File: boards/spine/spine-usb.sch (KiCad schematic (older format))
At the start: 4 parts, among them P1 USB_B, U1 FT2232H

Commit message: Get the BOM started
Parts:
- L1, L2: MfgId (none) -> CIB21P260NE; MfrId (none) -> Samsung; RefPrice1k (none) -> 0.00906; Vend1 (none) -> Digikey; Vend1Id (none) -> 1276-6342-2-ND
- P1: MfgId (none) -> E8144-B02022-L; MfrId (none) -> Pulse; RefPrice1k (none) -> 0.28; Vend1 (none) -> Digikey; Vend1Id (none) -> 553-2272-ND
- U1: MfgId (none) -> FT2232HL-REEL; MfrId (none) -> FTDI; RefPrice1k (none) -> 3.70; Vend1 (none) -> Digikey; Vend1Id (none) -> 768-1024-1-ND
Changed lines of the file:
@@
 F 1 "FT2232H" H 6650 5700 50  0000 L CNN
 F 2 "" H 5900 3600 50  0000 C CNN
-F 3 "" H 5900 3600 50  0000 C CNN
+F 3 "http://www.ftdichip.com/Support/Documents/DataSheets/ICs/DS_FT2232H.pdf" H 5900 3600 50  0000 C CNN
+F 4 "3.70" H 5900 3600 60  0001 C CNN "RefPrice1k"
+F 5 "768-1024-1-ND" H 5900 3600 60  0001 C CNN "Vend1Id"
+F 6 "FTDI" H 5900 3600 60  0001 C CNN "MfrId"
+F 7 "FT2232HL-REEL" H 5900 3600 60  0001 C CNN "MfgId"
+F 8 "Digikey" H 5900 3600 60  0001 C CNN "Vend1"
 	1    5900 3600
 	1    0    0    -1
@@
 F 1 "USB_B" H 2200 2650 50  0000 C CNN
 F 2 "" V 2200 2350 60  0000 C CNN
-F 3 "" V 2200 2350 60  0000 C CNN
+F 3 "http://productfinder.pulseeng.com/products/datasheets/E8144-B02022-L.PDF" V 2200 2350 60  0001 C CNN
+F 4 "Digikey" H 2250 2450 60  0001 C CNN "Vend1"
+F 5 "553-2272-ND" H 2250 2450 60  0001 C CNN "Vend1Id"
+F 6 "0.28" H 2250 2450 60  0001 C CNN "RefPrice1k"
+F 7 "Pulse" H 2250 2450 60  0001 C CNN "MfrId"
+F 8 "E8144-B02022-L" H 2250 2450 60  0001 C CNN "MfgId"
 	1    2250 2450
 	0    -1   1    0
@@
 FIFO_DATA[0..7]
 $Comp
-L FERRITE_BEAD L1
-U 1 1 56380FD6
-P 2750 1800
-F 0 "L1" H 2900 1850 50  0000 C BNN
-F 1 "FERRITE_BEAD" H 2900 1725 50  0000 C BNN
-F 2 "" H 2750 1950 50  0001 C CNN
-F 3 "" H 2775 1800 60  0000 C CNN
-	1    2750 1800
-	0    1    1    0
-$EndComp
-$Comp
 L FERRITE_BEAD L2
 U 1 1 5638109A
 P 2750 2700
 F 0 "L2" H 2900 2750 50  0000 C BNN
-F 1 "FERRITE_BEAD" H 2900 2625 50  0000 C BNN
+F 1 "FERRITE_BEAD" H 2900 2625 50  0001 C BNN
 F 2 "" H 2750 2850 50  0001 C CNN
-F 3 "" H 2775 2700 60  0000 C CNN
+F 3 "http://www.samsungsem.com/kr/front/downloadcms.do?path=/kr/support/product-search/bead/__icsFiles/afieldfile/2014/11/13&fileName=S_CIB21P110NE.pdf" H 2775 2700 60  0001 C CNN
+F 4 "0.00906" H 2750 2700 60  0001 C CNN "RefPrice1k"
+F 5 "Samsung" H 2750 2700 60  0001 C CNN "MfrId"
+F 6 "CIB21P260NE" H 2750 2700 60  0001 C CNN "MfgId"
+F 7 "Digikey" H 2750 2700 60  0001 C CNN "Vend1"
+F 8 "1276-6342-2-ND" H 2750 2700 60  0001 C CNN "Vend1Id"
 	1    2750 2700
 	0    1    1    0
@@
 Note TI's recommendations on USB grounding and EMI:\nhttp://www.ti.com/sc/docs/apps/msp/intrface/usb/emitest.pdf
 $Comp
-L GND #PWR1
+L GND #PWR01
 U 1 1 563811A6
 P 2150 3250
-F 0 "#PWR1" H 2150 3000 50  0001 C CNN
+F 0 "#PWR01" H 2150 3000 50  0001 C CNN
 F 1 "GND" H 2150 3100 50  0000 C CNN
 F 2 "" H 2150 3250 60  0000 C CNN
@@
 	2150 3200 2750 3200
 Connection ~ 2150 3200
+$Comp
+L FERRITE_BEAD L1
+U 1 1 563F5CD5
+P 2750 1800
+F 0 "L1" H 2900 1850 50  0000 C BNN
+F 1 "FERRITE_BEAD" H 2900 1725 50  0001 C BNN
+F 2 "" H 2750 1950 50  0001 C CNN
+F 3 "http://www.samsungsem.com/kr/front/downloadcms.do?path=/kr/support/product-search/bead/__icsFiles/afieldfile/2014/11/13&fileName=S_CIB21P110NE.pdf" H 2775 1800 60  0001 C CNN
+F 4 "0.00906" H 2750 1800 60  0001 C CNN "RefPrice1k"
+F 5 "Samsung" H 2750 1800 60  0001 C CNN "MfrId"
+F 6 "CIB21P260NE" H 2750 1800 60  0001 C CNN "MfgId"
+F 7 "Digikey" H 2750 1800 60  0001 C CNN "Vend1"
+F 8 "1276-6342-2-ND" H 2750 1800 60  0001 C CNN "Vend1Id"
+	1    2750 1800
+	0    1    1    0
+$EndComp
 $EndSCHEMATC

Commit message: Fuss with the USB
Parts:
- removed L2: FERRITE_BEAD, symbol FERRITE_BEAD
- added C? (x2): 0.1uF, symbol C
- added C? (x2): 10uF, symbol C
- added FB2: Ferrite bead, symbol FERRITE_BEAD
- added R? (x2): 4.7k, symbol R
- added R?: 10k, symbol R
- added R?: 12k 1%, symbol R
- FB1: renamed from L1; value FERRITE_BEAD -> Ferrite bead
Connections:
- net labels added: +3V3, VBUS_OUT, VBUS_SENSE
- wire segments 15 -> 68
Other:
- note added: "Todo: pick an ESD solution"
- note removed: "Note TI's recommendations on USB grounding and EMI:\nhttp://www.ti.com/sc/docs/apps/msp/intrface/usb/emitest.pdf"
- moved on the sheet: FB1, P1, U1

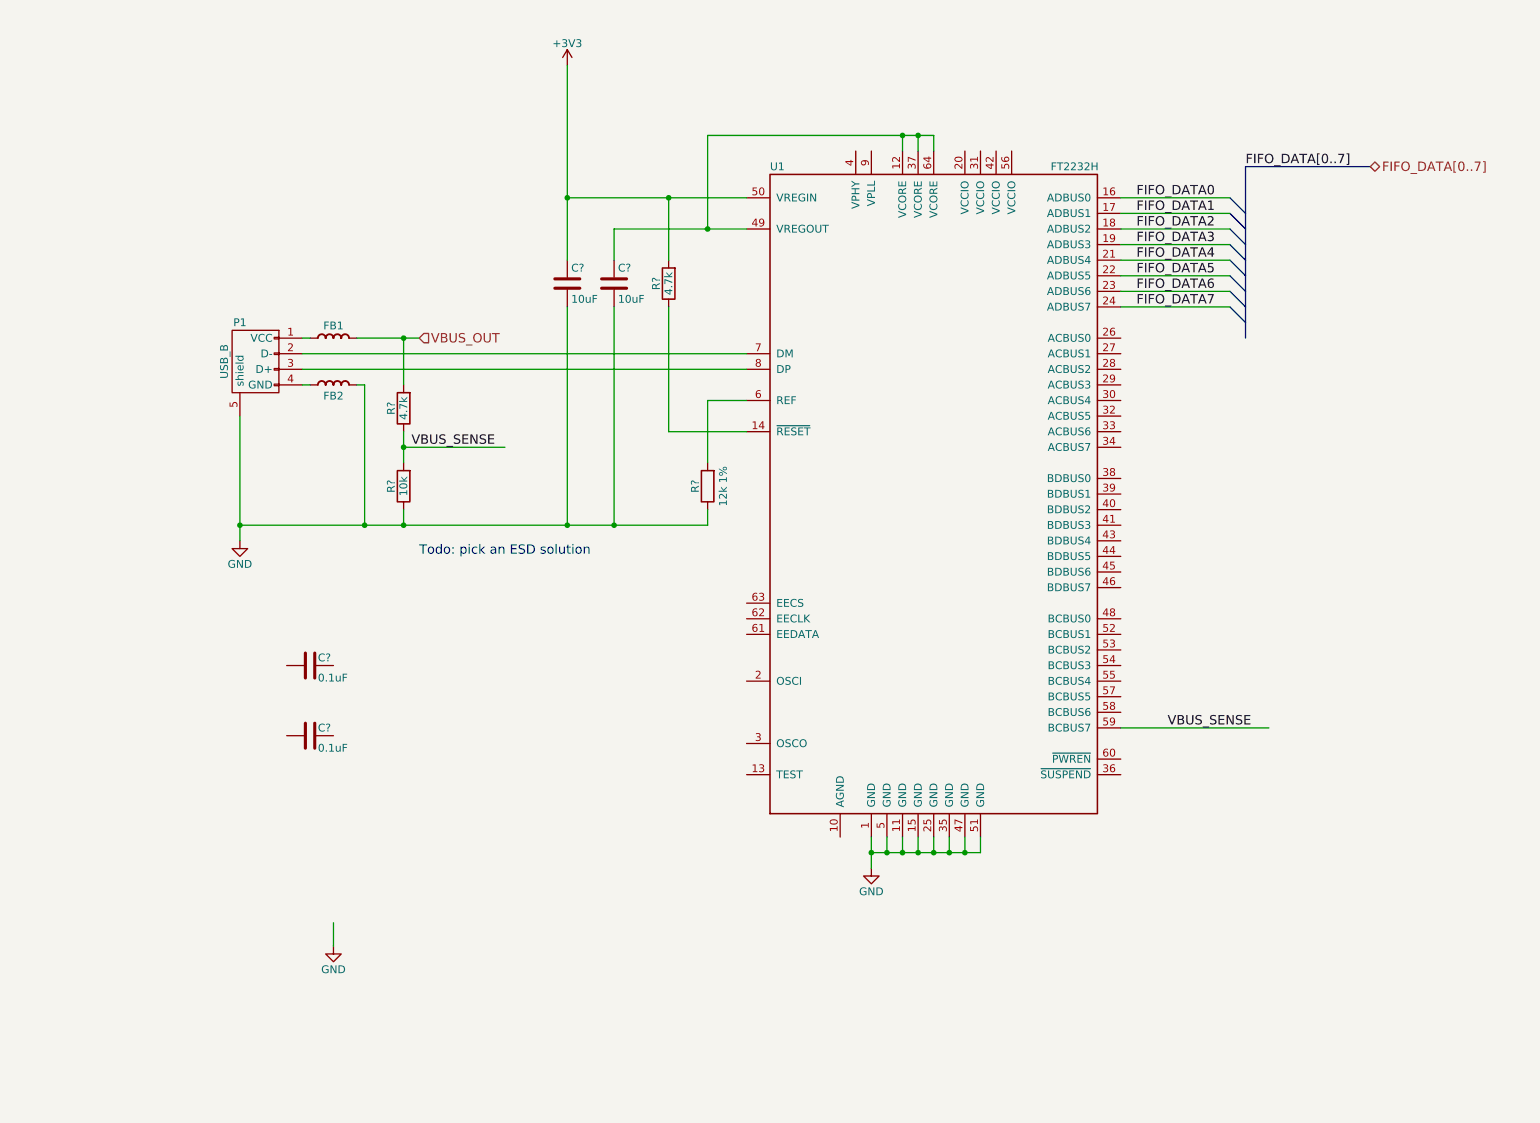
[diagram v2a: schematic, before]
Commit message: USB port: ESD, crystal, eeprom
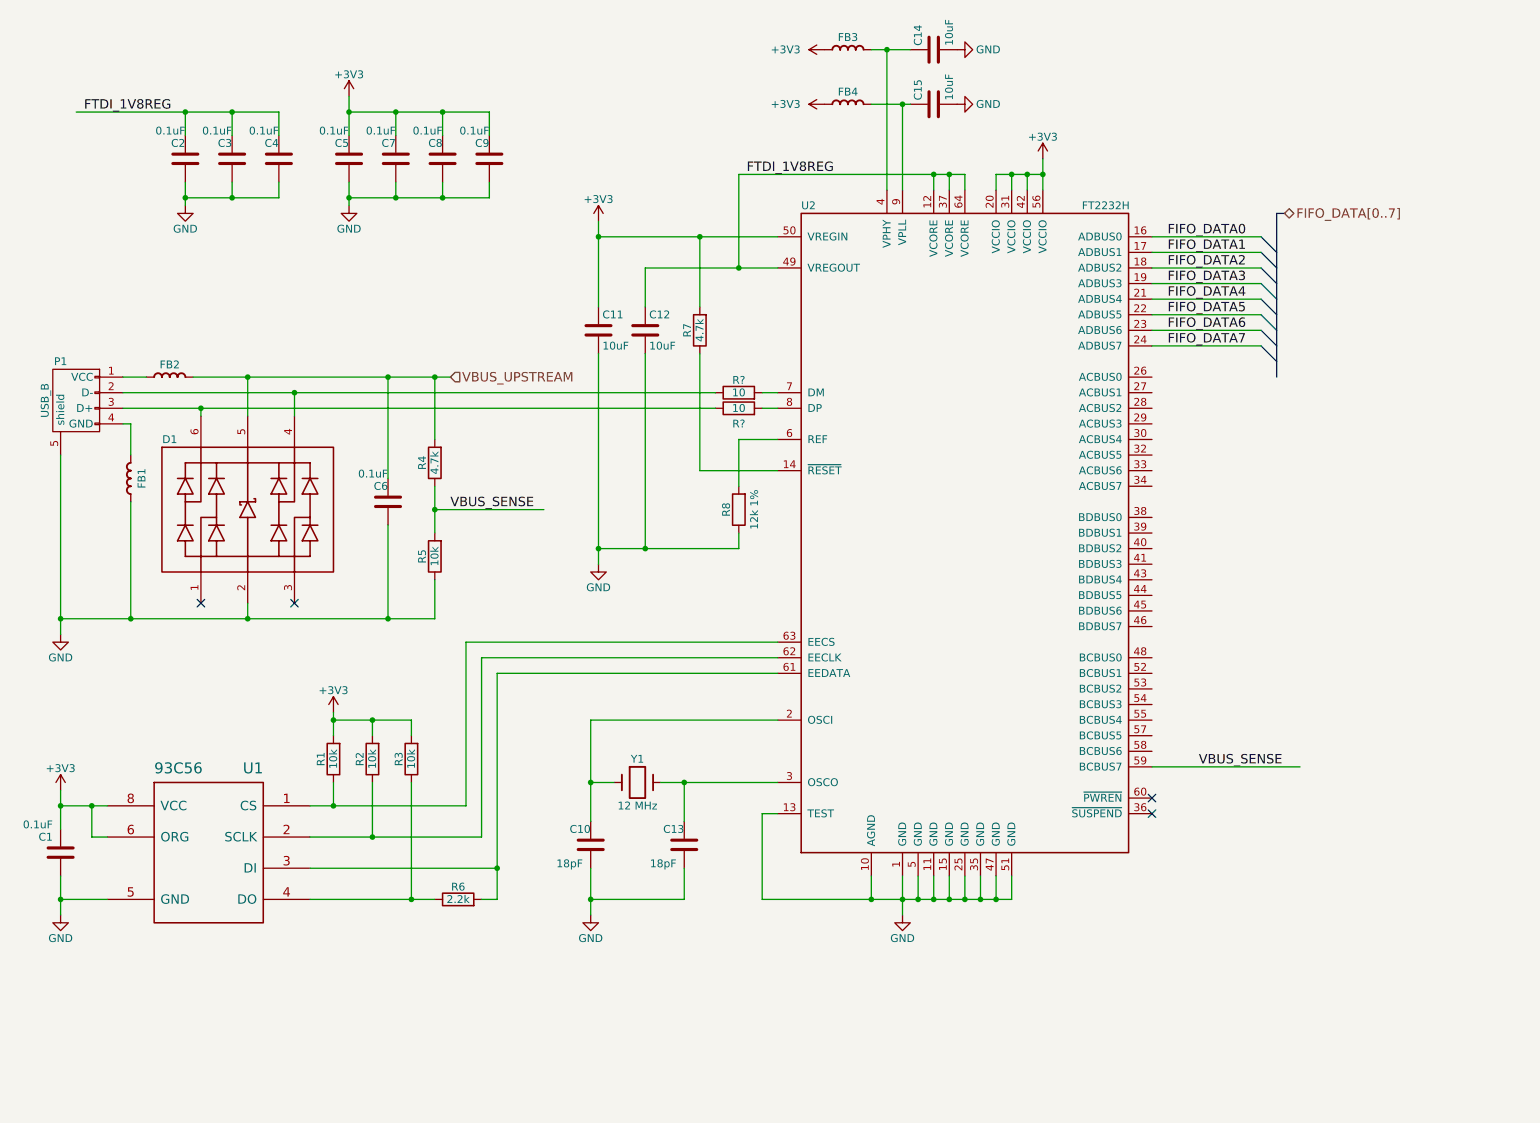
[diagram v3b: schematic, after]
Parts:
- removed C?: 0.1uF, symbol C
- removed C?: 10uF, symbol C
- added C1, C2, C3, C4, C5, C7, C8, C9: 0.1uF, symbol C
- added C10, C13: 18pF, symbol C
- added C11, C14, C15: 10uF, symbol C
- added D1: TVS DIODE 5.5VWM, symbol TVS_QUAD_STEERING
- added FB3, FB4: Ferrite bead, symbol FERRITE_BEAD
- added R1, R2, R3: 10k, symbol R
- added R6: 2.2k, symbol R
- added R? (x2): 10, symbol R
- added U1: 93C56, symbol 93C46
- added Y1: 12 MHz, symbol Crystal
- gave numbers to parts that had none: 6
- renumbered FB2 to FB1, FB1 to FB2, U1 to U2
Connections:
- net labels added: FTDI_1V8REG, VBUS_UPSTREAM
- net labels removed: VBUS_OUT
- wire segments 68 -> 119
- no-connect marks 0 -> 4
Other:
- note removed: "Todo: pick an ESD solution"
- moved on the sheet: C12, C6, FB1, FB2, P1, R4, R5, R7, R8, U2
